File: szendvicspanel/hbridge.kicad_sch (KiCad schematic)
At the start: 10 parts, among them Q3 BS170, Q4 BS170, Q5 BS250, Q6 BS250, Q7 BS170, Q8 BS170

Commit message: Footprintek
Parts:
- R10, R7, R8, R9: footprint (none) -> Resistor_THT:R_Axial_DIN0204_L3.6mm_D1.6mm_P5.08mm_Horizontal
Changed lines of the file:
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@@
 			)
 		)
-		(property "Footprint" ""
+		(property "Footprint" "Resistor_THT:R_Axial_DIN0204_L3.6mm_D1.6mm_P5.08mm_Horizontal"
 			(at 101.6 118.618 90)
 			(effects
@@
 			)
 		)
-		(property "Footprint" ""
+		(property "Footprint" "Resistor_THT:R_Axial_DIN0204_L3.6mm_D1.6mm_P5.08mm_Horizontal"
 			(at 47.498 119.38 90)
 			(effects
@@
 			)
 		)
-		(property "Footprint" ""
+		(property "Footprint" "Resistor_THT:R_Axial_DIN0204_L3.6mm_D1.6mm_P5.08mm_Horizontal"
 			(at 101.6 108.458 90)
 			(effects
@@
 			)
 		)
-		(property "Footprint" ""
+		(property "Footprint" "Resistor_THT:R_Axial_DIN0204_L3.6mm_D1.6mm_P5.08mm_Horizontal"
 			(at 64.008 119.38 90)
 			(effects

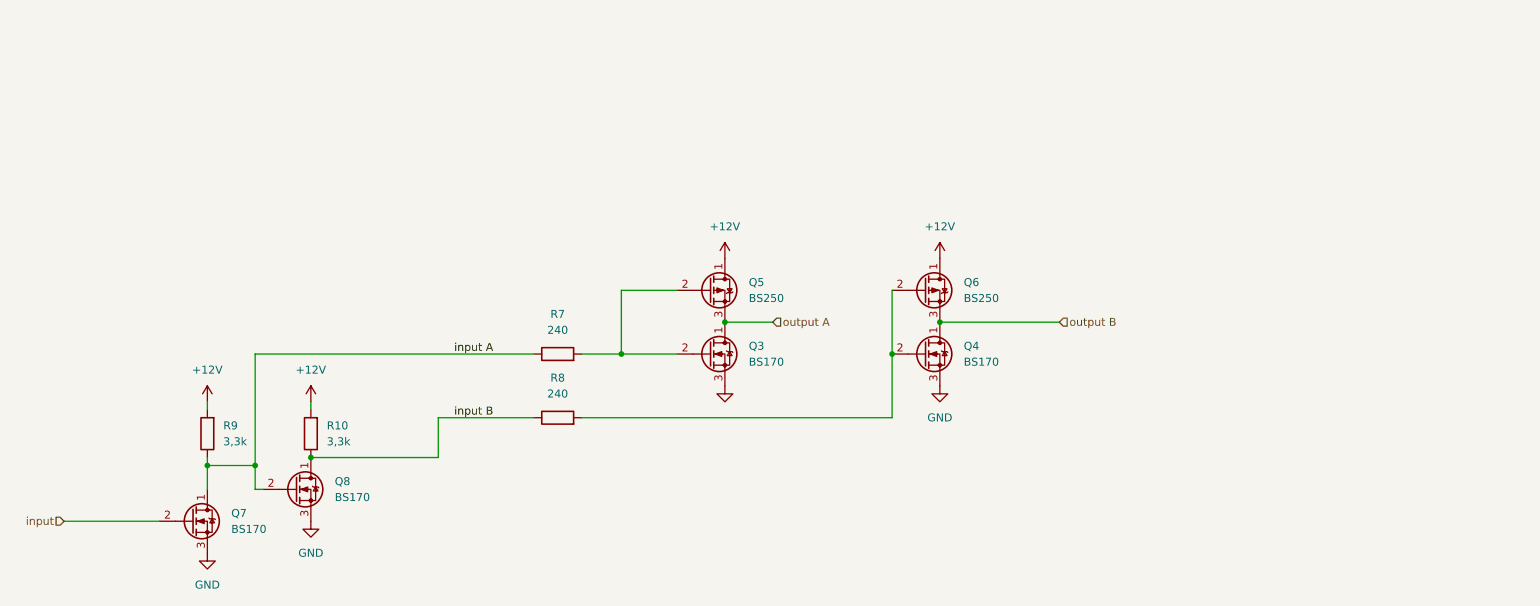
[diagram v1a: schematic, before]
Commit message: Jelgenerátor layer, README, .gitignore
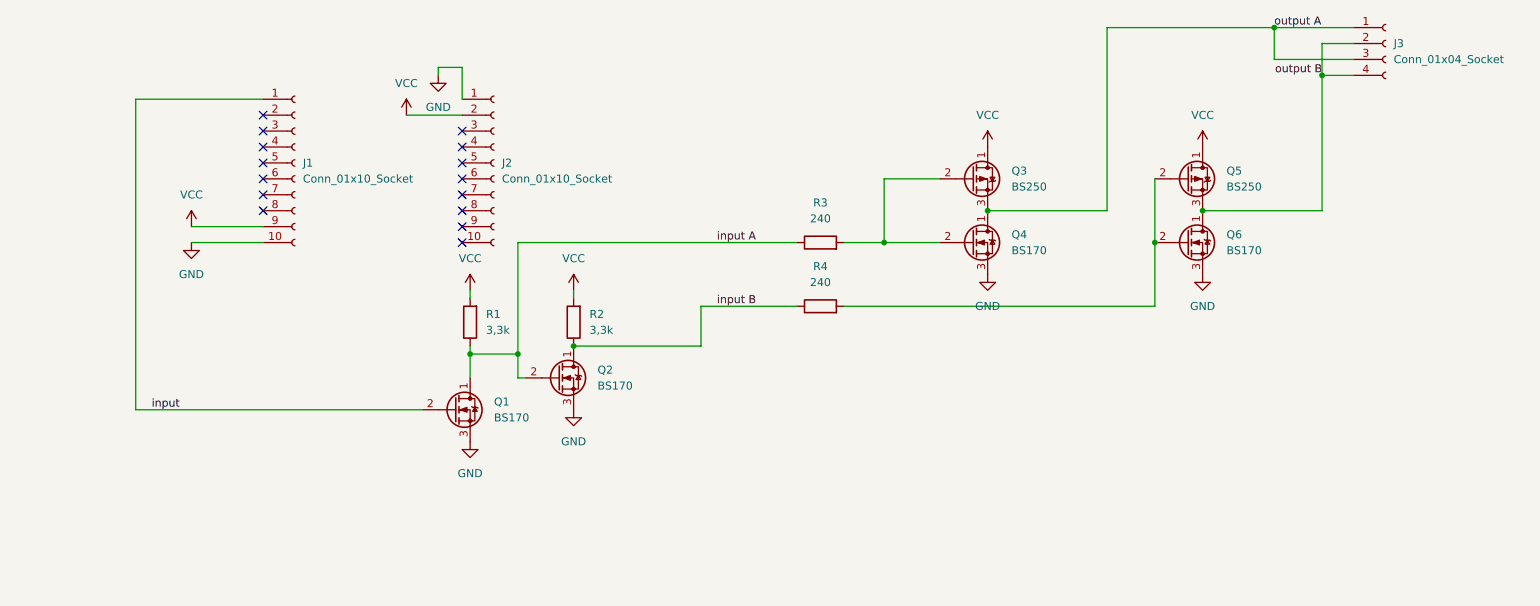
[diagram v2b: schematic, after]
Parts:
- added J1, J2: Conn_01x10_Socket, Connector_PinHeader_2.54mm:PinHeader_1x10_P2.54mm_Vertical, symbol Connector:Conn_01x10_Socket
- added J3: Conn_01x04_Socket, Connector_PinHeader_2.54mm:PinHeader_1x04_P2.54mm_Horizontal, symbol Connector:Conn_01x04_Socket
- renumbered Q7 to Q1, Q8 to Q2, Q5 to Q3, Q3 to Q4, Q6 to Q5, Q4 to Q6, R9 to R1, R10 to R2, R7 to R3, R8 to R4
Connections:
- net GND: now also J1.10 (Pin_10), J2.1 (Pin_1)
- net input: now also J1.1 (Pin_1)
- net output A: now also J3.1 (Pin_1), J3.3 (Pin_3)
- net output B: now also J3.2 (Pin_2), J3.4 (Pin_4)
- net +12V renamed VCC
- net VCC: now also J1.9 (Pin_9), J2.2 (Pin_2)
- no-connect marks 0 -> 15
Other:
- moved on the sheet: Q1, Q2, Q3, Q4, Q5, Q6, R1, R2, R3, R4
